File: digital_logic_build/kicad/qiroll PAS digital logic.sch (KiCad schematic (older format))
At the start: 47 parts, among them J2 led_sw1, J3 accessory, J4 mode_thr_batt, J5 3_pin, U1 4093B, U2 4027B, U3 4093B, U5 4093B, U6 14538B, U7 MCP1799_3V3

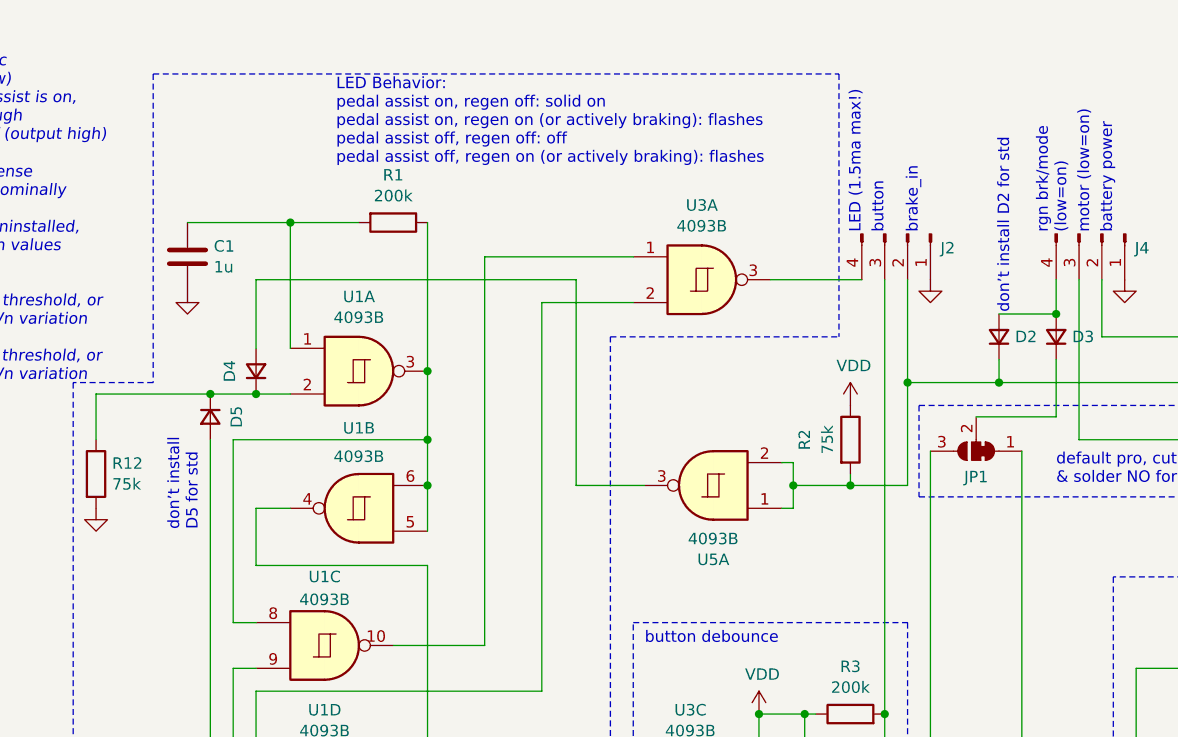
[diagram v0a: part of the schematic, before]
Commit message: clarify silkscreen
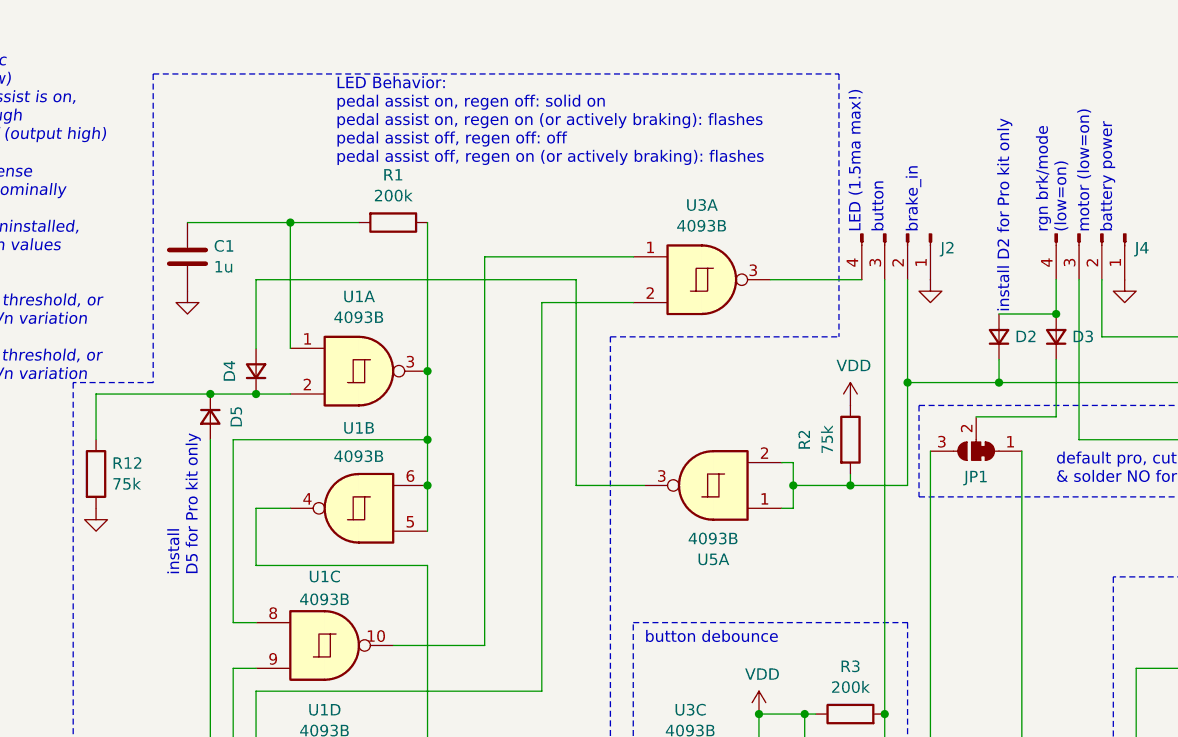
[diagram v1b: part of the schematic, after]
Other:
- note added: "install D2 for Pro kit only"
- note added: "install\nD5 for Pro kit only"
- note removed: "don’t install D2 for std"
- note removed: "don’t install\nD5 for std"
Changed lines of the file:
@@
 accessory_gnd
 Text Notes 5750 1650 1    50   ~ 0
-don’t install D2 for std
+install D2 for Pro kit only
 Wire Wire Line
 	3450 1400 4100 1400
@@
 Wire Wire Line
 	9150 4200 10600 4200
-Text Notes 2200 2600 1    50   ~ 0
-don’t install\nD5 for std
+Text Notes 2200 2800 1    50   ~ 0
+install\nD5 for Pro kit only
 $EndSCHEMATC

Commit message: even tidier schematic
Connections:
- net at U1.9, U2.1 (Q): now also U5.8; no longer U5.9
- net at U2.12 (R), U3.11: now also U5.9; no longer U5.8
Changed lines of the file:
@@
 Text Notes 550  1950 0    50   Italic 0
 note: pedal cadence sense\ncadence threshold is nominally\n40rpm on/29rpm off, \nwith C6 installed, C5 uninstalled,\nand typical 4093 Vp/Vn values\n(Vp = 3.3, Vn = 2.3)\n\ninstall C5+C6 to lower threshold, or\nmake up for 4093 Vp/Vn variation\n\ninstall C5 only to raise threshold, or\nmake up for 4093 Vp/Vn variation\n
-Text Notes 6900 4650 0    50   ~ 0
+Text Notes 6900 4450 0    50   ~ 0
 pedal
-Text Notes 6350 4200 0    50   ~ 0
+Text Notes 7150 5250 1    50   ~ 0
 pedal assist on
 $Comp
@@
 	2000 600  5000 600
 Wire Notes Line
-	6200 2800 6200 4950
-Wire Notes Line
-	6200 4950 7200 4950
-Wire Notes Line
-	7200 4950 7200 3500
+	6200 2800 6200 5400
+Wire Notes Line
+	6200 5400 7200 5400
+Wire Notes Line
+	7200 5400 7200 3500
 Wire Notes Line
 	7200 3500 7850 3500
@@
 Connection ~ 9050 3400
 Wire Wire Line
-	7300 4650 7300 5500
+	7300 4450 7300 5500
 Connection ~ 8850 4050
 Wire Wire Line
@@
 	2250 2200 2250 4250
 Wire Wire Line
-	7300 4650 6900 4650
+	7300 4450 6900 4450
 Wire Wire Line
 	6300 4050 6300 4550
@@
 $EndComp
 Wire Wire Line
-	7150 5300 7150 4450
-Wire Wire Line
-	7150 4450 6900 4450
-Wire Wire Line
 	5700 5300 7150 5300
 Wire Notes Line
@@
 	8150 3950 7300 3950
 Wire Wire Line
-	7300 3950 7300 4650
-Connection ~ 7300 4650
+	7300 3950 7300 4450
+Connection ~ 7300 4450
 Wire Notes Line
 	5350 2450 6750 2450
@@
 	9000 2600 9000 2550
 $Comp
-L power:VDD #PWR?
+L power:VDD #PWR0104
 U 1 1 622AB00C
 P 9050 3100
-F 0 "#PWR?" H 9050 2950 50  0001 C CNN
+F 0 "#PWR0104" H 9050 2950 50  0001 C CNN
 F 1 "VDD" H 9065 3273 50  0000 C CNN
 F 2 "" H 9050 3100 50  0001 C CNN
@@
 Text Notes 2200 2800 1    50   ~ 0
 install\nD5 for Pro kit only
+Wire Wire Line
+	7150 4650 6900 4650
+Wire Wire Line
+	7150 4650 7150 5300
 $EndSCHEMATC
